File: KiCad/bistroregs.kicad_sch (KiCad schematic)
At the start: 34 parts, among them U4 TDA38826XUMA1, U5 TDA38826XUMA1

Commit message: Add logo, other cool stuff
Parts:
- added C25, C26: 47uF, Capacitor_SMD:C_0805_2012Metric, symbol Device:C_Small
- added C27: 22uF, Capacitor_SMD:C_0805_2012Metric, symbol Device:C_Small
- added L3: 1uH, Inductor_SMD:L_Murata_DFE201610P, symbol Device:L_Small
- added U6: FAN49100AUC330X, Package_CSP:WLCSP-20_1.994x1.94mm_Layout4x5_P0.4mm, symbol Stormbreaker:FAN49100AUC330X
- C15, C22: Mouser https://au.mouser.com/ProductDetail/KYOCERA-AVX/KGM21AR51A4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 -> (none)
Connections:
- net EN: now also U6.A2 (EN)
- net GND: now also C25.2, C26.2, C27.2, U6.B1 (P_{GND}), U6.B2 (PT), U6.C1 (P_{GND}), U6.C2 (P_{GND}), U6.C3 (P_{GND}), U6.C4 (P_{GND}), U6.D1 (P_{GND}), U6.D2 (MODE), U6.E1 (A_{GND})
- net VCC renamed P_{VIN}
- net P_{VIN}: now also C27.1, U6.A1 (A_{VIN}), U6.A3 (P_{VIN}), U6.A4 (P_{VIN})
- new net: L3.1, U6.B3 (SW_{1}), U6.B4 (SW_{1})
- new net: L3.2, U6.D3 (SW_{2}), U6.D4 (SW_{2})
- new net +3.3V: C25.1, C26.1, U6.E3 (V_{OUT}), U6.E4 (V_{OUT})
- new net 3V3_PGOOD: U6.E2 (P_{GOOD})

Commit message: Rename project to "cafebara"
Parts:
- U4, U5: footprint Stormbreaker:TDA38826XUMA1 -> cafebara:TDA38826XUMA1
- U6: symbol Stormbreaker:FAN49100AUC330X -> cafebara:FAN49100AUC330X
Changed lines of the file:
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@@
 			)
 		)
-		(property "Footprint" "Stormbreaker:TDA38826XUMA1"
+		(property "Footprint" "cafebara:TDA38826XUMA1"
 			(at 87.63 188.9 0)
 			(effects
@@
 	)
 	(symbol
-		(lib_id "Stormbreaker:FAN49100AUC330X")
+		(lib_id "cafebara:FAN49100AUC330X")
 		(at 63.5 176.53 0)
 		(unit 1)
@@
 			)
 		)
-		(property "Footprint" "Stormbreaker:TDA38826XUMA1"
+		(property "Footprint" "cafebara:TDA38826XUMA1"
 			(at 88.9 117.78 0)
 			(effects

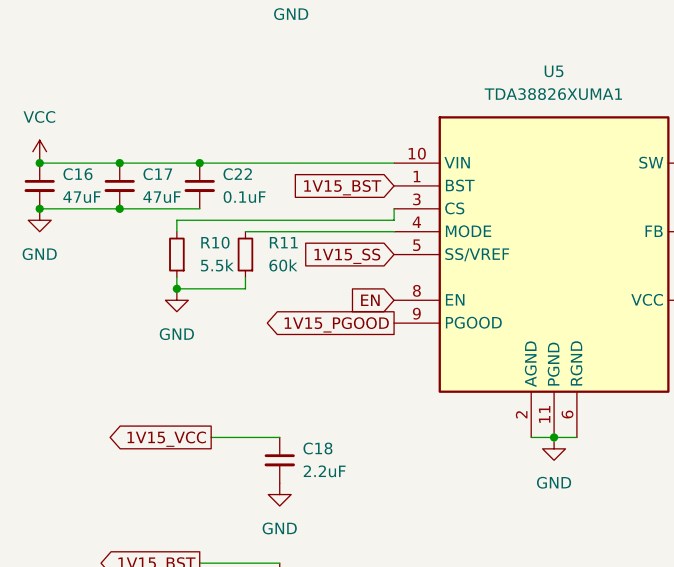
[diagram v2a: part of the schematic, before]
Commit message: Split regs into separate KiCad project
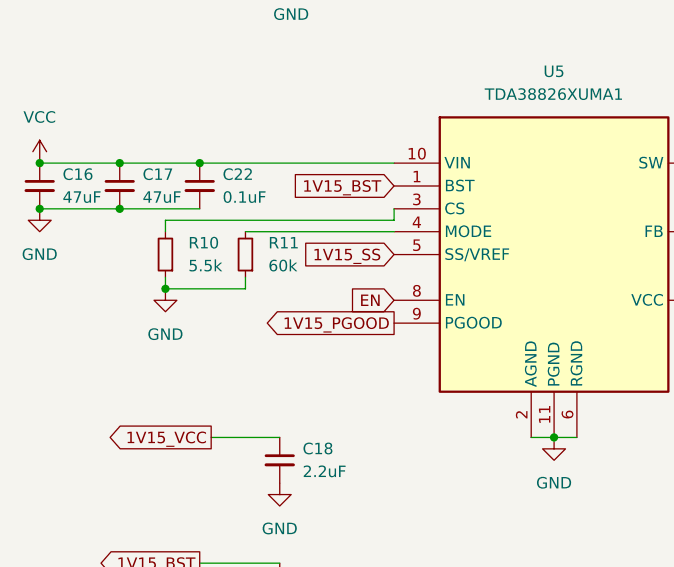
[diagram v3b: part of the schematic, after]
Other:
- moved on the sheet: R10
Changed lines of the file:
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@@
+	)
+	(junction
+		(at 30.48 110.49)
+		(diameter 0)
+		(color 0 0 0 0)
 	)
 	(junction
@@
 	)
 	(junction
-		(at 31.75 110.49)
-		(diameter 0)
-		(color 0 0 0 0)
-	)
-	(junction
 		(at 63.5 190.5)
 		(diameter 0)
@@
 	(wire
 		(pts
-			(xy 31.75 110.49) (xy 39.37 110.49)
-		)
-		(stroke
-			(width 0)
-			(type default)
-		)
-	)
-	(wire
-		(pts
 			(xy 100.33 33.02) (xy 107.95 33.02)
 		)
@@
 	(wire
 		(pts
-			(xy 31.75 102.87) (xy 31.75 104.14)
+			(xy 30.48 102.87) (xy 30.48 104.14)
 		)
 		(stroke
@@
 	(wire
 		(pts
+			(xy 30.48 110.49) (xy 39.37 110.49)
+		)
+		(stroke
+			(width 0)
+			(type default)
+		)
+	)
+	(wire
+		(pts
 			(xy 99.06 99.06) (xy 106.68 99.06)
 		)
@@
 	(wire
 		(pts
-			(xy 55.88 102.87) (xy 31.75 102.87)
+			(xy 55.88 102.87) (xy 30.48 102.87)
 		)
 		(stroke
@@
 	(wire
 		(pts
-			(xy 31.75 110.49) (xy 31.75 109.22)
+			(xy 30.48 110.49) (xy 30.48 109.22)
 		)
 		(stroke
@@
 	(symbol
 		(lib_id "power:GND")
-		(at 31.75 110.49 0)
+		(at 30.48 110.49 0)
 		(unit 1)
 		(exclude_from_sim no)
@@
 		(fields_autoplaced yes)
 		(property "Reference" "#PWR041"
-			(at 31.75 116.84 0)
+			(at 30.48 116.84 0)
 			(effects
 				(font
@@
 		)
 		(property "Value" "GND"
-			(at 31.75 115.57 0)
+			(at 30.48 115.57 0)
 			(effects
 				(font
@@
 		)
 		(property "Footprint" ""
-			(at 31.75 110.49 0)
+			(at 30.48 110.49 0)
 			(effects
 				(font
@@
 		)
 		(property "Datasheet" ""
-			(at 31.75 110.49 0)
+			(at 30.48 110.49 0)
 			(effects
 				(font
@@
 		)
 		(property "Description" "Power symbol creates a global label with name \"GND\" , ground"
-			(at 31.75 110.49 0)
+			(at 30.48 110.49 0)
 			(effects
 				(font
@@
 	(symbol
 		(lib_id "Device:R_Small")
-		(at 31.75 106.68 180)
+		(at 30.48 106.68 180)
 		(unit 1)
 		(exclude_from_sim no)
@@
 		(fields_autoplaced yes)
 		(property "Reference" "R10"
-			(at 34.29 105.4099 0)
+			(at 33.02 105.4099 0)
 			(effects
 				(font
@@
 		)
 		(property "Value" "5.5k"
-			(at 34.29 107.9499 0)
+			(at 33.02 107.9499 0)
 			(effects
 				(font
@@
 		)
 		(property "Footprint" "Resistor_SMD:R_0402_1005Metric"
-			(at 31.75 106.68 0)
+			(at 30.48 106.68 0)
 			(effects
 				(font
@@
 		)
 		(property "Datasheet" "~"
-			(at 31.75 106.68 0)
+			(at 30.48 106.68 0)
 			(effects
 				(font
@@
 		)
 		(property "Description" "Resistor, small symbol"
-			(at 31.75 106.68 0)
-			(effects
-				(font
+			(at 30.48 106.68 0)
+			(effects
+				(font
